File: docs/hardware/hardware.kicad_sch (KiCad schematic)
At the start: 17 parts, among them J1 BASYS_JA, J2 AudioJack2, J3 GAMEPAD, J6 BASYS_JB, J7 GAMEPAD_1, J8 GAMEPAD_2, SW1 LEFT, SW2 UP, SW3 RIGHT, SW4 PRIMARY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

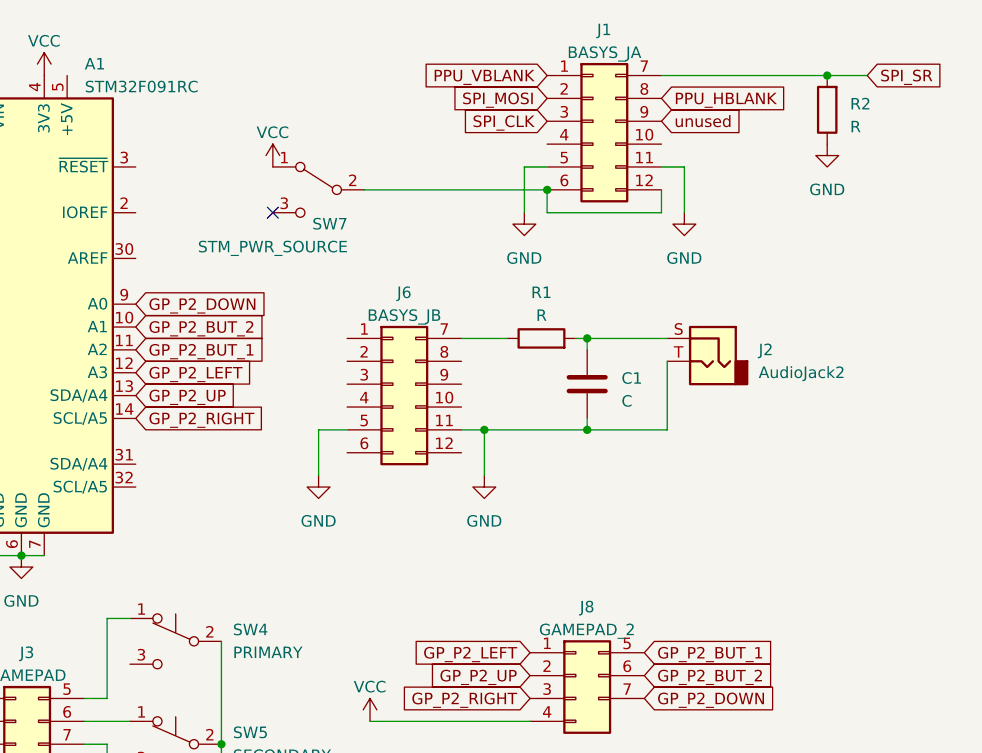
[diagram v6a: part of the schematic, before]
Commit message: remove pull down resistor for SPI SR and test new SPI transmit
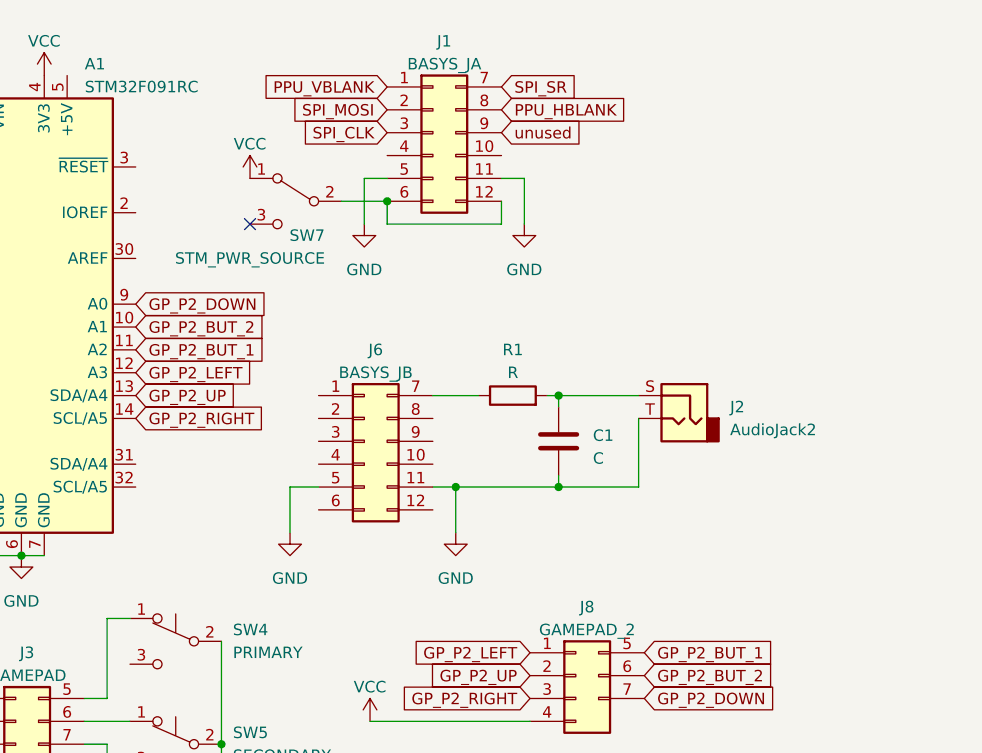
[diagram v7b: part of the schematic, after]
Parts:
- removed R2: R, Resistor_THT:R_Axial_DIN0207_L6.3mm_D2.5mm_P7.62mm_Horizontal, symbol Device:R
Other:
- moved on the sheet: C1, J1, J2, J6, R1, SW7
